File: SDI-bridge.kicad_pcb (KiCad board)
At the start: 4 copper layers, 60 x 30 mm, 108 parts, among them J1 22-23-2021, J2 543630489, J3 031-70526-21, U1 GS2971A, U2 MAX8902B, Y1 ABM7_27.000MH_D2Y_T

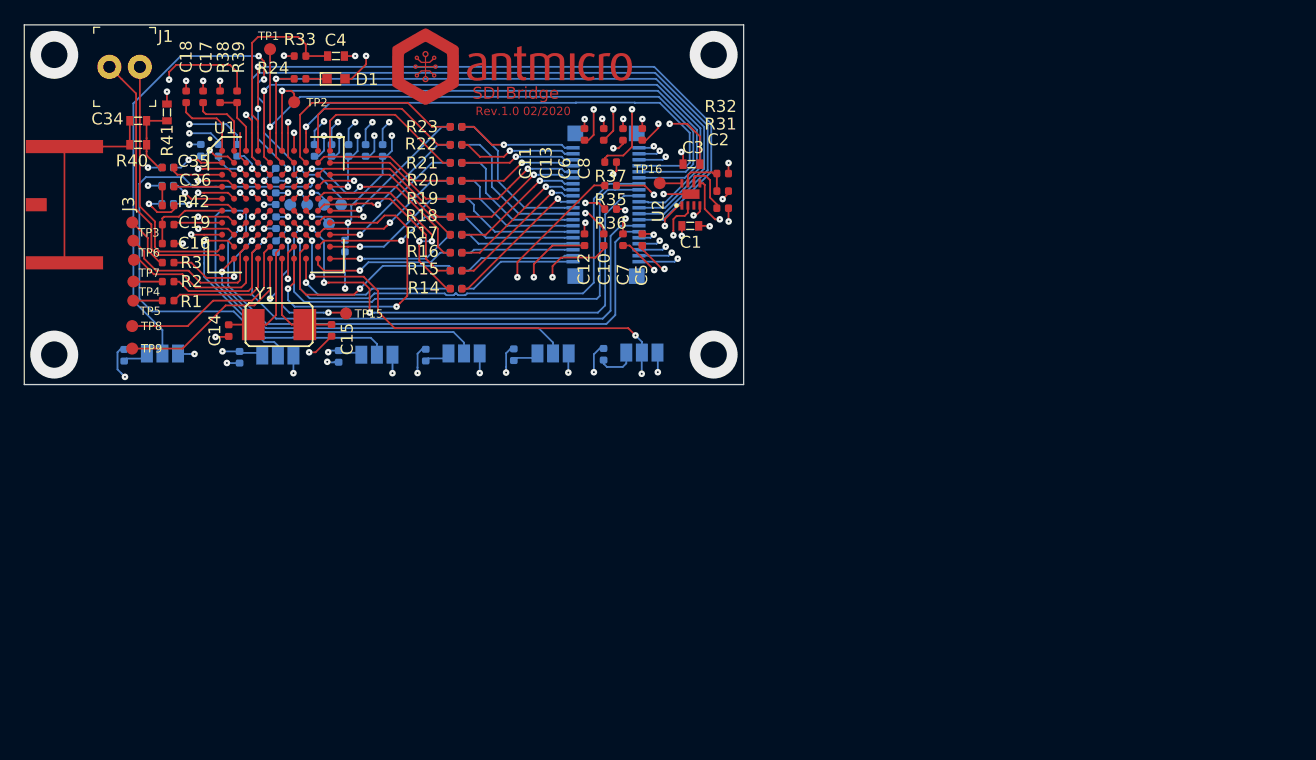
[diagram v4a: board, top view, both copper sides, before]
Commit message: Initial component placement and outline definition
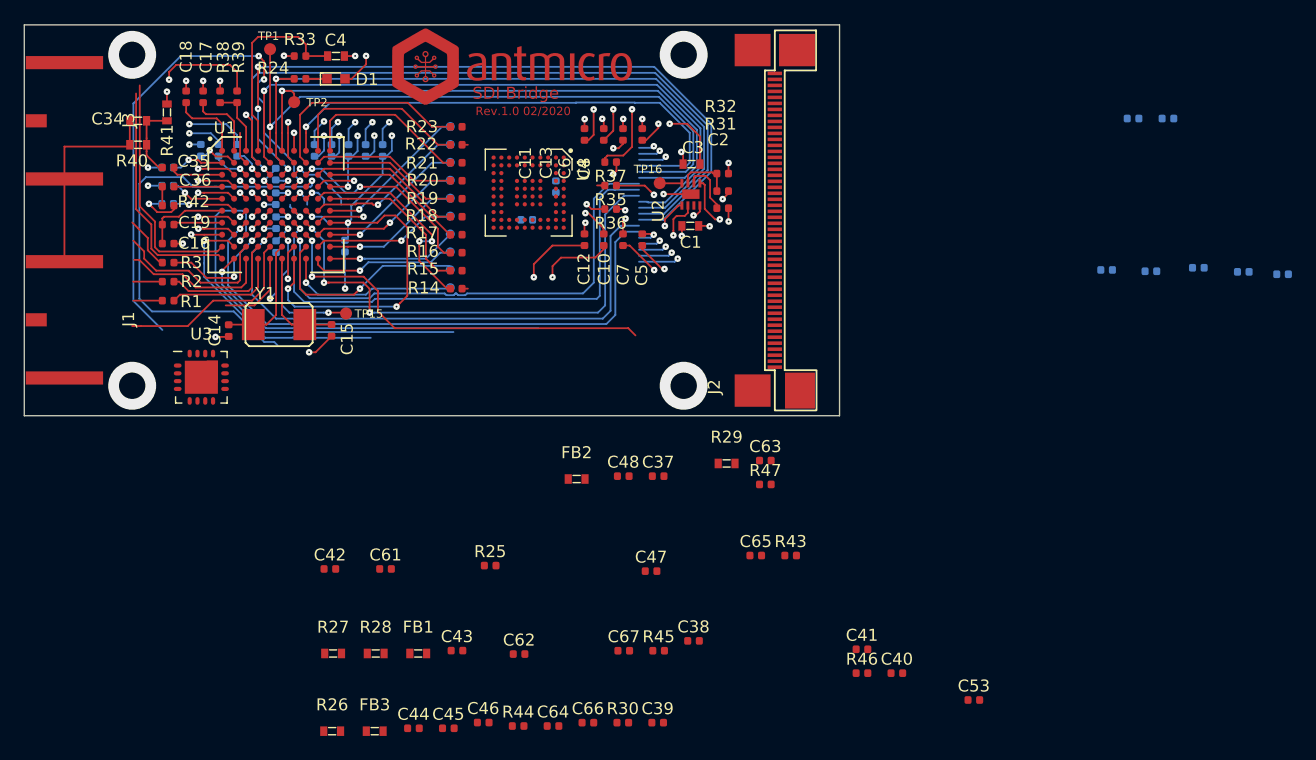
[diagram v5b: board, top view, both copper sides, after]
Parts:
- removed JP1, JP2, JP3, JP4, JP5, JP6: SolderJumper_3_Open, Jumper:SolderJumper-3_P1.3mm_Open_Pad1.0x1.5mm
- removed R10, R11, R12, R13, R4, R5, R6, R7, R8, R9: R_0R_0402, antmicro-footprints:0402-res
- removed TP13, TP14: TP_SMD1MM, antmicro-footprints:Testpoint_smd_1mm
- added C37: C_10n_0402, antmicro-footprints:0402-cap, F.Cu at (152.9, 137.6)
- added C38: C_10n_0402, antmicro-footprints:0402-cap, F.Cu at (155.8, 151.4)
- added C39: C_10n_0402, antmicro-footprints:0402-cap, F.Cu at (152.8, 158.2)
- added C40: C_4u7_0402, antmicro-footprints:0402-cap, F.Cu at (172.8, 154.1)
- added C41: C_1u_0402, antmicro-footprints:0402-cap, F.Cu at (169.9, 152.1)
- added C42: C_5n6_0402, antmicro-footprints:0402-res, F.Cu at (125.5, 145.4)
- added C43: C_1u_0402, antmicro-footprints:0402-cap, F.Cu at (136.1, 152.2)
- added C44: C_4u7_0402, antmicro-footprints:0402-cap, F.Cu at (132.5, 158.7)
- added C45: C_10n_0402, antmicro-footprints:0402-cap, F.Cu at (135.4, 158.7)
- added C46: C_10n_0402, antmicro-footprints:0402-cap, F.Cu at (138.3, 158.2)
- added C47: C_2n2_0402, antmicro-footprints:0402-cap, F.Cu at (152.3, 145.6)
- added C48: C_100n_0402_6V3, antmicro-footprints:0402-cap, F.Cu at (150.0, 137.6)
- added C49: C_100n_0402_6V3, antmicro-footprints:0402-cap, B.Cu at (194.0, 120.5)
- added C50: C_100n_0402_6V3, antmicro-footprints:0402-cap, B.Cu at (197.9, 120.3)
- added C51: C_100n_0402_6V3, antmicro-footprints:0402-cap, B.Cu at (201.7, 120.6)
- added C52: C_100n_0402_6V3, antmicro-footprints:0402-cap, B.Cu at (204.9, 120.8)
- added C53: C_2u2_0402, antmicro-footprints:0402-cap, F.Cu at (179.2, 156.3)
- added C57: C_100n_0402_6V3, antmicro-footprints:0402-cap, B.Cu at (144.3, 113.5)
- added C58: C_100n_0402_6V3, antmicro-footprints:0402-cap, B.Cu at (141.9, 116.3)
- added C59: C_100n_0402_6V3, antmicro-footprints:0402-cap, B.Cu at (195.4, 107.8)
- added C60: C_100n_0402_6V3, antmicro-footprints:0402-cap, B.Cu at (192.5, 107.8)
- added C61: C_100n_0402_6V3, antmicro-footprints:0402-cap, F.Cu at (130.1, 145.4)
- added C62: C_4u7_0402, antmicro-footprints:0402-cap, F.Cu at (141.3, 152.5)
- added C63: C_100n_0402_6V3, antmicro-footprints:0402-cap, F.Cu at (161.8, 136.3)
- added C64: C_1u_0402, antmicro-footprints:0402-cap, F.Cu at (144.1, 158.5)
- added C65: C_4u7_0402, antmicro-footprints:0402-cap, F.Cu at (161.0, 144.3)
- added C66: C_1u_0402, antmicro-footprints:0402-cap, F.Cu at (147.0, 158.2)
- added C67: C_100n_0402_6V3, antmicro-footprints:0402-cap, F.Cu at (150.0, 152.2)
- added FB1: BLM18PG121SN1D, antmicro-footprints:0603-res, F.Cu at (132.9, 152.4)
- added FB2: BLM18PG121SN1D, antmicro-footprints:0603-res, F.Cu at (146.1, 137.9)
- added FB3: BLM18PG121SN1D, antmicro-footprints:0603-res, F.Cu at (129.2, 158.9)
- added R43: R_0R_0402, antmicro-footprints:0402-res, F.Cu at (163.9, 144.3)
- added R44: R_4k7_0402, antmicro-footprints:0402-res, F.Cu at (141.2, 158.5)
- added R45: R_4k7_0402, antmicro-footprints:0402-res, F.Cu at (152.9, 152.2)
- added R46: R_2k37_0402, antmicro-footprints:0402-res, F.Cu at (169.9, 154.1)
- added R47: R_0R_0402, antmicro-footprints:0402-res, F.Cu at (161.8, 138.3)
- added R48: R_2k37_0402, antmicro-footprints:0402-res, B.Cu at (190.3, 120.4)
- added U3: GS2988, antmicro-footprints:QFN-16_EP_4x4_Pitch0.65mm, F.Cu at (114.8, 129.4)
- added U4: CrossLink_LIF-MD6000-6JMG80I, antmicro-footprints:BGA-80pin_ckfBGA80_7.0x7.0mm, F.Cu at (142.1, 114.0)
- J1: value 22-23-2021 -> 031-70526-21; footprint antmicro-footprints:PinHeader_1x2_P2.54mm_Drill1.02mm -> antmicro-footprints:BNC_Edge_Conn
- J2: value 543630489 -> WE_68715014522; footprint antmicro-footprints:543630489 -> antmicro-footprints:WE_68715014522; moved to F.Cu
- R25: value R_0R_0402 -> R_750R_0402; moved to F.Cu
- R26, R27, R28, R29: value R_0R_0402 -> R_75R_0603; footprint antmicro-footprints:0402-res -> antmicro-footprints:0603-res; moved to F.Cu
- R30: moved to F.Cu
- TP10, TP11, TP12: value TP_SMD1MM -> TP_SMD_0_75MM; footprint antmicro-footprints:Testpoint_smd_1mm -> antmicro-footprints:Testpoint_smd_0_75mm
- TP3, TP4, TP5, TP6, TP7, TP8, TP9: value TP_SMD1MM -> TP_SMD_0_75MM; footprint antmicro-footprints:Testpoint_smd_1mm -> antmicro-footprints:Testpoint_smd_0_75mm; moved to B.Cu
- moved R30 51.7 mm to (149.9, 158.2), turned to 0 degrees
- moved R26 32.3 mm to (125.7, 158.9), turned to 0 degrees
- moved R28 31.4 mm to (129.3, 152.4), turned to 0 degrees
- moved TP9 30.0 mm to (135.5, 113.0), turned to 90 degrees
- moved TP8 28.6 mm to (135.5, 114.5), turned to 90 degrees
- moved R25 27.2 mm to (138.9, 145.1), turned to 0 degrees
- moved TP3 27.0 mm to (135.5, 121.9), turned to 90 degrees
- moved TP5 26.7 mm to (135.5, 118.9), turned to 90 degrees
- moved TP7 26.6 mm to (135.5, 115.9), turned to 90 degrees
- moved TP6 26.4 mm to (135.5, 117.4), turned to 90 degrees
- moved TP4 26.4 mm to (135.5, 120.4), turned to 90 degrees
- moved R27 24.8 mm to (125.8, 152.4), turned to 0 degrees
- moved J1 22.0 mm to (101.0, 124.6), turned to 270 degrees
- moved R29 19.9 mm to (158.6, 136.6), turned to 0 degrees
- moved TP12 14.8 mm to (135.5, 108.5), turned to 90 degrees
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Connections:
- J1 pad 1: /~SDO~ -> Net-(C44-Pad1)
- J1 pad 2: /SDO -> GND
- J2 pad 1: +3V3 -> Net-(J2-Pad1)
- J2 pad 10: /F_DE -> Net-(J2-Pad10)
- J2 pad 11: /LOCKED -> Net-(J2-Pad11)
- J2 pad 12: /Y_1ANC -> GNDREF
- J2 pad 13: /DATA_ERRORb -> Net-(J2-Pad13)
- J2 pad 14: /TIM_861 -> Net-(J2-Pad14)
- J2 pad 15: /~RC_BYP~ -> GNDREF
- J2 pad 16: GNDREF -> Net-(J2-Pad16)
- J2 pad 17: GNDREF -> Net-(J2-Pad17)
- J2 pad 19: GNDREF -> /MIPI_D3_N
- J2 pad 2: +3V3 -> Net-(J2-Pad2)
- J2 pad 20: GNDREF -> /MIPI_D3_P
- J2 pad 21: /DOUT19 -> /MIPI_D2_N
- J2 pad 22: /DOUT18 -> /MIPI_D2_P
- J2 pad 23: /DOUT17 -> /MIPI_D1_N
- J2 pad 24: /DOUT16 -> /MIPI_D1_P
- J2 pad 25: /DOUT15 -> /MIPI_D0_N
- J2 pad 26: /DOUT14 -> /MIPI_D0_P
- J2 pad 27: /DOUT13 -> GNDREF
- J2 pad 28: /DOUT12 -> /MIPI_CLK_N
- J2 pad 29: /DOUT11 -> /MIPI_CLK_P
- J2 pad 3: +3V3 -> Net-(J2-Pad3)
- J2 pad 30: /DOUT10 -> GNDREF
- J2 pad 31: /DOUT9 -> Net-(J2-Pad31)
- J2 pad 32: /DOUT8 -> Net-(J2-Pad32)
- J2 pad 33: /DOUT7 -> /RST
- J2 pad 34: /DOUT6 -> Net-(J2-Pad34)
- J2 pad 35: /DOUT5 -> Net-(J2-Pad35)
- J2 pad 36: /DOUT4 -> Net-(J2-Pad36)
- J2 pad 37: /DOUT3 -> Net-(J2-Pad37)
- J2 pad 38: /DOUT2 -> Net-(J2-Pad38)
- J2 pad 39: /DOUT1 -> /SDA
- J2 pad 4: /PCLK -> Net-(J2-Pad4)
- J2 pad 40: /DOUT0 -> /SCL
- J2 pad 5: /H_HSYNC -> Net-(J2-Pad5)
- J2 pad 6: /V_VSYNC -> Net-(J2-Pad6)
- J2 pad 7: /20bit_~10bit~ -> Net-(J2-Pad7)
- J2 pad 8: /~SMPTE_BYPASS~ -> Net-(J2-Pad8)
- J2 pad 9: /DVB_ASI -> GNDREF
- R25 pad 1: Net-(JP1-Pad3) -> VDD
- R25 pad 2: GNDREF -> Net-(R25-Pad2)
- R26 pad 1: Net-(JP2-Pad3) -> Net-(C42-Pad2)
- R26 pad 2: GNDREF -> Net-(C42-Pad1)
- R27 pad 1: Net-(JP3-Pad3) -> Net-(C42-Pad2)
- R27 pad 2: GNDREF -> VDD
- R28 pad 2: GNDREF -> VDD
- R29 pad 1: Net-(JP5-Pad3) -> GNDA
- R29 pad 2: GNDREF -> Net-(C40-Pad2)
- R3 pad 1: /AUDIO_WORLD_CLK -> /AUDIO_WORD_CLK
- R30 pad 1: Net-(JP6-Pad3) -> +3V3
- R30 pad 2: GNDREF -> VDD
- TP10 pad 1: /SCLK_TCK -> /D7
- TP11 pad 1: /SDOUT_TDO -> /D8
- TP12 pad 1: /~CS~_TMS -> /D9
- TP3 pad 1: /AUDIO_WORLD_CLK -> /D0
- TP4 pad 1: /AUDIO_SERIAL_BIT_CLK -> /D1
- TP5 pad 1: /AUDIO_MASTER_CLK -> /D2
- TP6 pad 1: /AUDIO_OUTPUT_CH1_2 -> /D3
- TP7 pad 1: /AUDIO_OUTPUT_CH3_4 -> /D4
- TP8 pad 1: /AUDIO_OUTPUT_CH5_6 -> /D5
- TP9 pad 1: /AUDIO_OUTPUT_CH7_8 -> /D6
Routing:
- net /DOUT9: track 13.6 -> 0.00 mm
- net /DOUT8: track 13.1 -> 0.00 mm
- net /DOUT7: track 12.4 -> 0.00 mm
- net GNDREF: track 77.1 -> 65.0 mm, vias 39 -> 34
- net /DOUT11: track 12.1 -> 0.00 mm, vias 1 -> 0
- net /DOUT10: track 12.5 -> 0.49 mm, vias 1 -> 0
- net /DOUT12: track 11.6 -> 0.00 mm, vias 1 -> 0
- net /DOUT6: track 11.4 -> 0.00 mm
- net /DOUT13: track 11.2 -> 0.00 mm, vias 1 -> 0
- net /DOUT14: track 10.8 -> 0.00 mm, vias 1 -> 0
- net /DOUT5: track 10.7 -> 0.00 mm
- net +3.3VA: track 44.5 -> 33.9 mm, vias 8 -> 7
- net /DOUT15: track 10.4 -> 0.00 mm, vias 1 -> 0
- net /DOUT0: track 10.2 -> 0.00 mm
- net /DOUT4: track 10.0 -> 0.00 mm
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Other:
- board size 60 x 30 mm -> 68 x 32.6 mm

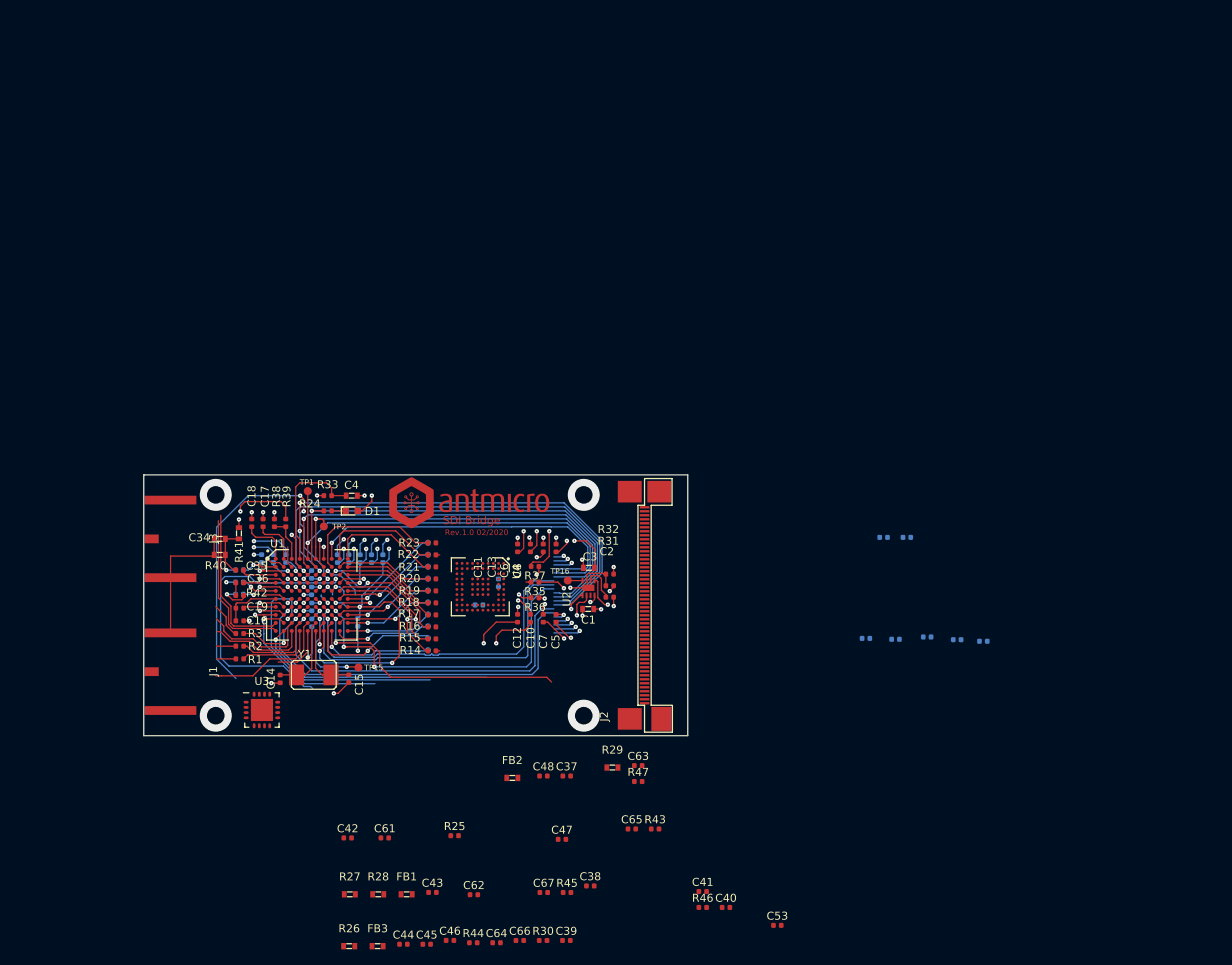
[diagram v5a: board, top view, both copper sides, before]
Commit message: Expose DPHY1 at FFC connector
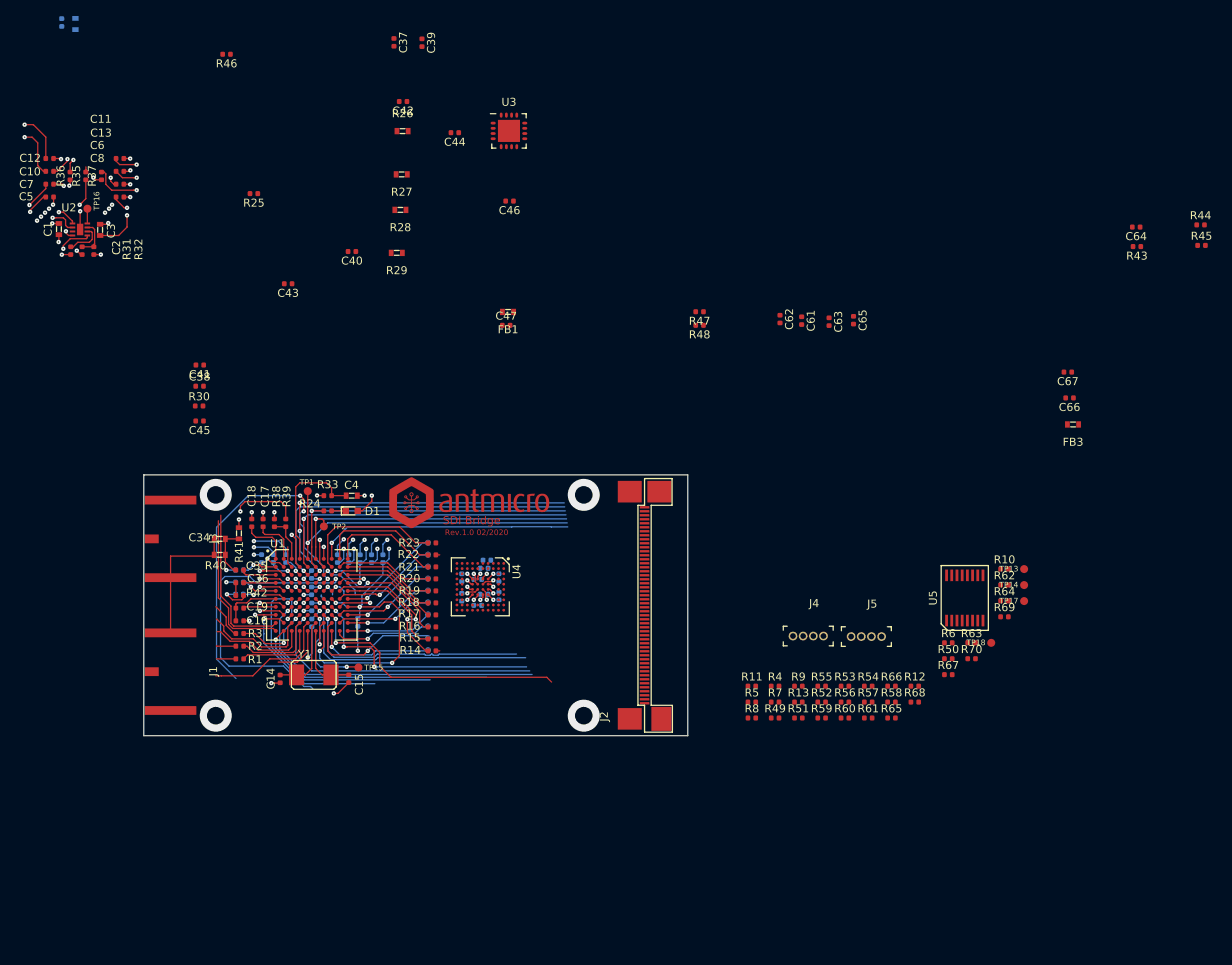
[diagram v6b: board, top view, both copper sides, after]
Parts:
- added J4: MC-HVT1-S04-G, antmicro-footprints:PinHeader_1x4_P1.27mm_Drill.7mm, F.Cu at (181.2, 120.1)
- added J5: MC-HVT1-S04-G, antmicro-footprints:PinHeader_1x4_P1.27mm_Drill.7mm, F.Cu at (188.4, 120.2)
- added R10: R_0R_0402, antmicro-footprints:0402-res, F.Cu at (207.6, 111.8)
- added R11: R_0R_0402, antmicro-footprints:0402-res, F.Cu at (176.0, 126.4)
- added R12: R_0R_0402, antmicro-footprints:0402-res, F.Cu at (196.4, 126.4)
- added R13: R_0R_0402, antmicro-footprints:0402-res, F.Cu at (181.8, 128.4)
- added R4: R_2k37_0402, antmicro-footprints:0402-res, F.Cu at (178.9, 126.4)
- added R49: R_0R_0402, antmicro-footprints:0402-res, F.Cu at (178.9, 130.4)
- added R5: R_2k37_0402, antmicro-footprints:0402-res, F.Cu at (176.0, 128.4)
- added R50: R_0R_0402, antmicro-footprints:0402-res, F.Cu at (200.6, 123.0)
- added R51: R_0R_0402, antmicro-footprints:0402-res, F.Cu at (181.8, 130.4)
- added R52: R_0R_0402, antmicro-footprints:0402-res, F.Cu at (184.7, 128.4)
- added R53: R_0R_0402, antmicro-footprints:0402-res, F.Cu at (187.7, 126.4)
- added R54: R_0R_0402, antmicro-footprints:0402-res, F.Cu at (190.6, 126.4)
- added R55: R_0R_0402, antmicro-footprints:0402-res, F.Cu at (184.7, 126.4)
- added R56: R_0R_0402, antmicro-footprints:0402-res, F.Cu at (187.7, 128.4)
- added R57: R_0R_0402, antmicro-footprints:0402-res, F.Cu at (190.6, 128.4)
- added R58: R_0R_0402, antmicro-footprints:0402-res, F.Cu at (193.5, 128.4)
- added R59: R_0R_0402, antmicro-footprints:0402-res, F.Cu at (184.7, 130.4)
- added R6: R_0R_0402, antmicro-footprints:0402-res, F.Cu at (200.6, 121.0)
- added R60: R_0R_0402, antmicro-footprints:0402-res, F.Cu at (187.7, 130.4)
- added R61: R_0R_0402, antmicro-footprints:0402-res, F.Cu at (190.6, 130.4)
- added R62: R_0R_0402, antmicro-footprints:0402-res, F.Cu at (207.6, 113.8)
- added R63: R_2k37_0402, antmicro-footprints:0402-res, F.Cu at (203.5, 121.0)
- added R64: R_2k37_0402, antmicro-footprints:0402-res, F.Cu at (207.6, 115.8)
- added R65: R_0R_0402, antmicro-footprints:0402-res, F.Cu at (193.5, 130.4)
- added R66: R_2k37_0402, antmicro-footprints:0402-res, F.Cu at (193.5, 126.4)
- added R67: R_0R_0402, antmicro-footprints:0402-res, F.Cu at (200.6, 125.0)
- added R68: R_0R_0402, antmicro-footprints:0402-res, F.Cu at (196.4, 128.4)
- added R69: R_0R_0402, antmicro-footprints:0402-res, F.Cu at (207.6, 117.7)
- added R7: R_2k37_0402, antmicro-footprints:0402-res, F.Cu at (178.9, 128.4)
- added R70: R_0R_0402, antmicro-footprints:0402-res, F.Cu at (203.5, 123.0)
- added R8: R_0R_0402, antmicro-footprints:0402-res, F.Cu at (176.0, 130.4)
- added R9: R_0R_0402, antmicro-footprints:0402-res, F.Cu at (181.8, 126.4)
- added TP13: TP_SMD1MM, antmicro-footprints:Testpoint_smd_1mm, F.Cu at (210.0, 111.8)
- added TP14: TP_SMD1MM, antmicro-footprints:Testpoint_smd_1mm, F.Cu at (210.0, 113.8)
- added TP17: TP_SMD1MM, antmicro-footprints:Testpoint_smd_1mm, F.Cu at (210.0, 115.8)
- added TP18: TP_SMD1MM, antmicro-footprints:Testpoint_smd_1mm, F.Cu at (205.9, 121.0)
- added U5: SC18IS602BIPW, antmicro-footprints:SC18IS602B, F.Cu at (202.6, 115.4)
- C48, C53, FB2: moved to B.Cu
- R48: moved to F.Cu
- moved C53 144.0 mm to (89.7, 43.5), turned to 270 degrees
- moved R44 127.7 mm to (232.1, 68.8)
- moved R46 122.1 mm to (110.3, 47.4), turned to 180 degrees
- moved C64 120.0 mm to (224.1, 69.0), turned to 180 degrees
- moved C39 113.7 mm to (134.8, 46.0), turned to 270 degrees
- moved R45 113.3 mm to (232.2, 71.3)
- moved FB2 108.9 mm to (91.5, 43.6), turned to 90 degrees
- moved FB3 108.7 mm to (216.2, 93.7), turned to 180 degrees
- moved R26 102.1 mm to (132.3, 57.0)
- moved C44 101.6 mm to (138.9, 57.2), turned to 180 degrees
- moved C66 96.5 mm to (215.7, 90.4), turned to 180 degrees
- moved R43 94.5 mm to (224.1, 71.5), turned to 180 degrees
- moved C40 94.4 mm to (126.0, 72.1), turned to 180 degrees
- moved C37 94.2 mm to (131.3, 45.9), turned to 270 degrees
- moved C46 92.7 mm to (145.7, 65.8), turned to 180 degrees
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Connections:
- C47 pad 1: +3V3 -> /VCCIO
- C48 pad 1: /VCCIO_0 -> /VCCIO
- C49 pad 1: /VCCIO_0 -> /VCCIO
- C50 pad 1: /VCCIO_0 -> /VCCIO
- C51 pad 1: /VCCIO_0 -> /VCCIO
- C52 pad 1: /VCCIO_0 -> /VCCIO
- C53 pad 1: +1V2 -> /VCCA_DPHY
- C57 pad 1: /VCCA_DPHY0 -> /VCCA_DPHY
- C58 pad 1: /VCCA_DPHY0 -> /VCCA_DPHY
- C59 pad 1: /VCCA_DPHY0 -> /VCCA_DPHY
- C60 pad 1: /VCCA_DPHY0 -> /VCCA_DPHY
- FB1 pad 2: /VCCIO_0 -> /VCCIO
- FB2 pad 2: /VCCA_DPHY0 -> /VCCA_DPHY
- J2 pad 1: Net-(J2-Pad1) -> /MIPI1_D3_N
- J2 pad 10: Net-(J2-Pad10) -> /MIPI1_CLK_N
- J2 pad 11: Net-(J2-Pad11) -> /MIPI1_CLK_P
- J2 pad 19: /MIPI_D3_N -> /MIPI0_D3_N
- J2 pad 2: Net-(J2-Pad2) -> /MIPI1_D3_P
- J2 pad 20: /MIPI_D3_P -> /MIPI0_D3_P
- J2 pad 21: /MIPI_D2_N -> /MIPI0_D2_N
- J2 pad 22: /MIPI_D2_P -> /MIPI0_D2_P
- J2 pad 23: /MIPI_D1_N -> /MIPI0_D1_N
- J2 pad 24: /MIPI_D1_P -> /MIPI0_D1_P
- J2 pad 25: /MIPI_D0_N -> /MIPI0_D0_N
- J2 pad 26: /MIPI_D0_P -> /MIPI0_D0_P
- J2 pad 28: /MIPI_CLK_N -> /MIPI0_CLK_N
- J2 pad 29: /MIPI_CLK_P -> /MIPI0_CLK_P
- J2 pad 3: Net-(J2-Pad3) -> /MIPI1_D2_N
- J2 pad 39: /SDA -> /SDA_GS
- J2 pad 4: Net-(J2-Pad4) -> /MIPI1_D2_P
- J2 pad 40: /SCL -> /SCL_GS
- J2 pad 41: Net-(J2-Pad41) -> /SDA_CL
- J2 pad 42: Net-(J2-Pad42) -> /SCL_CL
- J2 pad 5: Net-(J2-Pad5) -> /MIPI1_D1_N
- J2 pad 6: Net-(J2-Pad6) -> /MIPI1_D1_P
- J2 pad 7: Net-(J2-Pad7) -> /MIPI1_D0_N
- J2 pad 8: Net-(J2-Pad8) -> /MIPI1_D0_P
- R44 pad 2: /VCCIO_0 -> /VCCIO
- R45 pad 2: /VCCIO_0 -> /VCCIO
- R46 pad 1: /SCL -> /SCL_GS
- R48 pad 1: /SDA -> /SDA_GS
- U3 pad 10: Net-(U3-Pad10) -> GNDA
- U3 pad 17: Net-(U3-Pad17) -> GNDA
- U4 pad A1: Net-(U4-PadA1) -> /DPHY1_D2_N
- U4 pad A10: /MIPI_D3_N -> /DPHY0_D3_N
- U4 pad A2: Net-(U4-PadA2) -> /DPHY1_D0_N
- U4 pad A3: Net-(U4-PadA3) -> /DPHY1_CLK_N
- U4 pad A4: Net-(U4-PadA4) -> /DPHY1_D1_N
- U4 pad A5: Net-(U4-PadA5) -> /DPHY1_D3_N
- U4 pad A6: /MIPI_D2_N -> /DPHY0_D2_N
- U4 pad A7: /MIPI_D0_N -> /DPHY0_D0_N
- U4 pad A8: /MIPI_CLK_N -> /DPHY0_CLK_N
- U4 pad A9: /MIPI_D1_N -> /DPHY0_D1_N
- U4 pad B1: Net-(U4-PadB1) -> /DPHY1_D2_P
- U4 pad B10: /MIPI_D3_P -> /DPHY0_D3_P
- U4 pad B2: Net-(U4-PadB2) -> /DPHY1_D0_P
- U4 pad B3: Net-(U4-PadB3) -> /DPHY1_CLK_P
- U4 pad B4: Net-(U4-PadB4) -> /DPHY1_D1_P
- U4 pad B5: Net-(U4-PadB5) -> /DPHY1_D3_P
- U4 pad B6: /MIPI_D2_P -> /DPHY0_D2_P
- U4 pad B7: /MIPI_D0_P -> /DPHY0_D0_P
- U4 pad B8: /MIPI_CLK_P -> /DPHY0_CLK_P
- U4 pad B9: /MIPI_D1_P -> /DPHY0_D1_P
- U4 pad C2: Net-(U4-PadC2) -> GNDREF
- U4 pad D1: /SW_EN -> Net-(U4-PadD1)
- U4 pad D2: /VCCA_DPHY0 -> /VCCA_DPHY
- U4 pad D4: /VCCA_DPHY0 -> /VCCA_DPHY
- U4 pad D7: /VCCA_DPHY0 -> /VCCA_DPHY
- U4 pad E7: /VCCA_DPHY0 -> /VCCA_DPHY
- U4 pad F4: /VCCIO_0 -> /VCCIO
- U4 pad F5: /VCCIO_0 -> /VCCIO
- U4 pad F6: /VCCIO_0 -> /VCCIO
- U4 pad F7: /VCCIO_0 -> /VCCIO
- U4 pad G4: /VCCIO_0 -> /VCCIO
- U4 pad H1: /SCL -> /SCL_CL
- U4 pad H9: /Audio_EN_~DIS~ -> /SW_EN
- U4 pad J1: /SDA -> /SDA_CL
- U4 pad K2: /IOPROC_EN_~DIS~ -> Net-(U4-PadK2)
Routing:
- net /DATA_ERRORb: track 61.7 -> 43.3 mm
- net /Y_1ANC: track 59.6 -> 42.4 mm
- net /LOCKED: track 56.4 -> 40.4 mm
- net /F_DE: track 53.9 -> 39.2 mm
- net /V_VSYNC: track 51.0 -> 38.2 mm
- net /20bit_~10bit~: track 41.6 -> 29.0 mm
- net /~SMPTE_BYPASS~: track 44.0 -> 31.9 mm
- net /DVB_ASI: track 42.6 -> 30.7 mm
- net /H_HSYNC: track 53.5 -> 41.9 mm
- net /PCLK: track 42.7 -> 32.3 mm
- net /TIM_861: track 45.6 -> 35.7 mm
- net /~RC_BYP~: track 48.2 -> 38.7 mm
- net GNDREF: track 65.0 -> 55.7 mm, vias 34 -> 36
- net /VCCIO: track 0.00 -> 5.56 mm, vias 0 -> 5
- net +3V3: track 21.5 -> 16.9 mm, vias 9 -> 10
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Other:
- net class Default: clearance 0.15 -> 0.1; trace_width 0.15 -> 0.1
- rule trace_clearance: 0.15 -> 0.1
- rule trace_min: 0.15 -> 0.1
